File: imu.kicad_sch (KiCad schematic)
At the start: 6 parts, among them U6 LSM9DS1

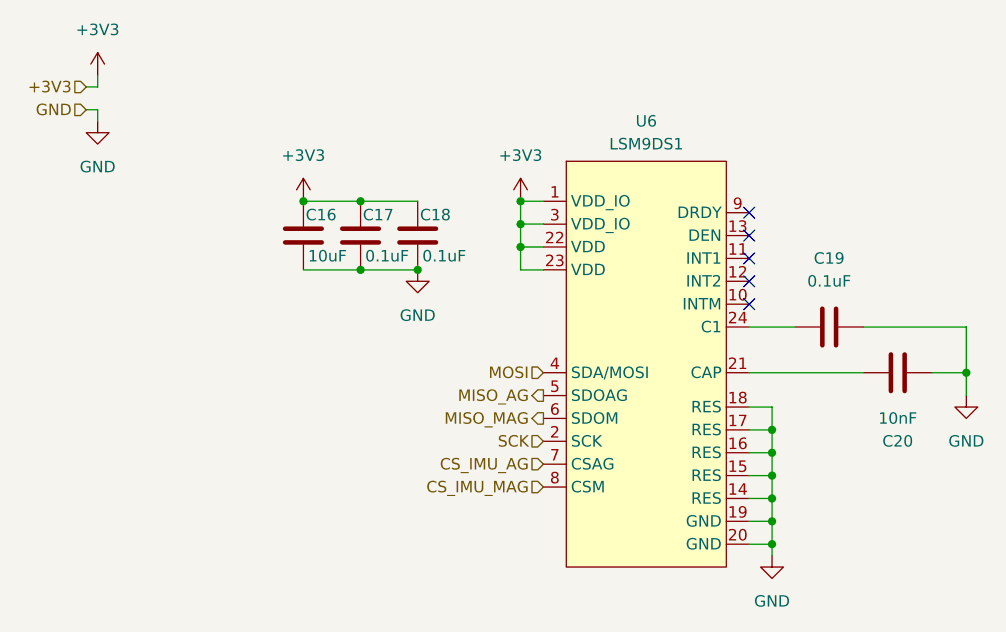
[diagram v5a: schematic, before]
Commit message: Radio footprint selection
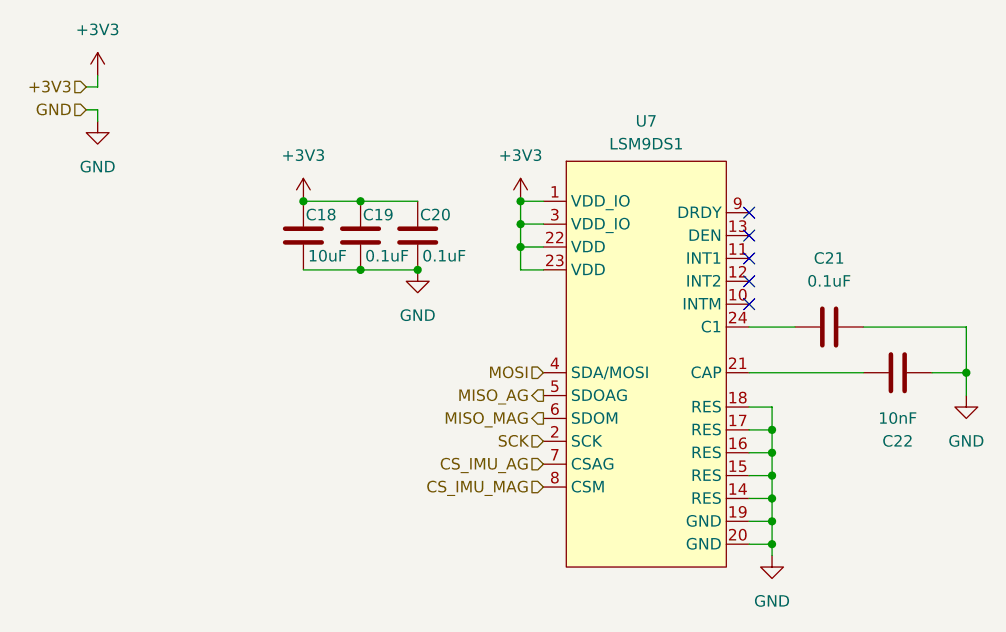
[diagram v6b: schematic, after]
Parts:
- renumbered C16 to C18, C17 to C19, C18 to C20, C19 to C21, C20 to C22, U6 to U7
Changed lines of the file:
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@@
 		(on_board yes)
 		(dnp no)
-		(property "Reference" "C16"
+		(property "Reference" "C18"
 			(at 76.454 49.784 0)
 			(effects
@@
 			(project ""
 				(path "/2c2eadf0-5503-4531-8753-1a232087fe8c/b9b0c40a-7771-4bc1-adbf-abe0201c34d0/6214bd7c-f0f2-4cad-9d95-7bb7bb29e083"
-					(reference "C16")
+					(reference "C18")
 					(unit 1)
 				)
@@
 		(dnp no)
 		(fields_autoplaced yes)
-		(property "Reference" "U6"
+		(property "Reference" "U7"
 			(at 114.3 39.37 0)
 			(effects
@@
 			(project ""
 				(path "/2c2eadf0-5503-4531-8753-1a232087fe8c/b9b0c40a-7771-4bc1-adbf-abe0201c34d0/6214bd7c-f0f2-4cad-9d95-7bb7bb29e083"
-					(reference "U6")
+					(reference "U7")
 					(unit 1)
 				)
@@
 		(dnp no)
 		(fields_autoplaced yes)
-		(property "Reference" "#PWR070"
+		(property "Reference" "#PWR076"
 			(at 76.2 52.07 0)
 			(effects
@@
 			(project ""
 				(path "/2c2eadf0-5503-4531-8753-1a232087fe8c/b9b0c40a-7771-4bc1-adbf-abe0201c34d0/6214bd7c-f0f2-4cad-9d95-7bb7bb29e083"
-					(reference "#PWR070")
+					(reference "#PWR076")
 					(unit 1)
 				)
@@
 		(dnp no)
 		(fields_autoplaced yes)
-		(property "Reference" "#PWR071"
+		(property "Reference" "#PWR077"
 			(at 100.33 52.07 0)
 			(effects
@@
 			(project ""
 				(path "/2c2eadf0-5503-4531-8753-1a232087fe8c/b9b0c40a-7771-4bc1-adbf-abe0201c34d0/6214bd7c-f0f2-4cad-9d95-7bb7bb29e083"
-					(reference "#PWR071")
+					(reference "#PWR077")
 					(unit 1)
 				)
@@
 		(dnp no)
 		(fields_autoplaced yes)
-		(property "Reference" "#PWR069"
+		(property "Reference" "#PWR075"
 			(at 53.34 45.72 0)
 			(effects
@@
 			(project ""
 				(path "/2c2eadf0-5503-4531-8753-1a232087fe8c/b9b0c40a-7771-4bc1-adbf-abe0201c34d0/6214bd7c-f0f2-4cad-9d95-7bb7bb29e083"
-					(reference "#PWR069")
+					(reference "#PWR075")
 					(unit 1)
 				)
@@
 		(dnp no)
 		(fields_autoplaced yes)
-		(property "Reference" "#PWR074"
+		(property "Reference" "#PWR080"
 			(at 128.27 93.98 0)
 			(effects
@@
 			(project ""
 				(path "/2c2eadf0-5503-4531-8753-1a232087fe8c/b9b0c40a-7771-4bc1-adbf-abe0201c34d0/6214bd7c-f0f2-4cad-9d95-7bb7bb29e083"
-					(reference "#PWR074")
+					(reference "#PWR080")
 					(unit 1)
 				)
@@
 		(dnp no)
 		(fields_autoplaced yes)
-		(property "Reference" "#PWR073"
+		(property "Reference" "#PWR079"
 			(at 149.86 76.2 0)
 			(effects
@@
 			(project ""
 				(path "/2c2eadf0-5503-4531-8753-1a232087fe8c/b9b0c40a-7771-4bc1-adbf-abe0201c34d0/6214bd7c-f0f2-4cad-9d95-7bb7bb29e083"
-					(reference "#PWR073")
+					(reference "#PWR079")
 					(unit 1)
 				)
@@
 		(on_board yes)
 		(dnp no)
-		(property "Reference" "C18"
+		(property "Reference" "C20"
 			(at 89.154 49.784 0)
 			(effects
@@
 			(project ""
 				(path "/2c2eadf0-5503-4531-8753-1a232087fe8c/b9b0c40a-7771-4bc1-adbf-abe0201c34d0/6214bd7c-f0f2-4cad-9d95-7bb7bb29e083"
-					(reference "C18")
+					(reference "C20")
 					(unit 1)
 				)
@@
 		(on_board yes)
 		(dnp no)
-		(property "Reference" "C17"
+		(property "Reference" "C19"
 			(at 82.804 49.784 0)
 			(effects
@@
 			(project ""
 				(path "/2c2eadf0-5503-4531-8753-1a232087fe8c/b9b0c40a-7771-4bc1-adbf-abe0201c34d0/6214bd7c-f0f2-4cad-9d95-7bb7bb29e083"
-					(reference "C17")
+					(reference "C19")
 					(unit 1)
 				)
@@
 		(dnp no)
 		(fields_autoplaced yes)
-		(property "Reference" "C19"
+		(property "Reference" "C21"
 			(at 134.62 54.61 90)
 			(effects
@@
 			(project ""
 				(path "/2c2eadf0-5503-4531-8753-1a232087fe8c/b9b0c40a-7771-4bc1-adbf-abe0201c34d0/6214bd7c-f0f2-4cad-9d95-7bb7bb29e083"
-					(reference "C19")
+					(reference "C21")
 					(unit 1)
 				)
@@
 		(on_board yes)
 		(dnp no)
-		(property "Reference" "C20"
+		(property "Reference" "C22"
 			(at 142.24 74.93 90)
 			(effects
@@
 			(project ""
 				(path "/2c2eadf0-5503-4531-8753-1a232087fe8c/b9b0c40a-7771-4bc1-adbf-abe0201c34d0/6214bd7c-f0f2-4cad-9d95-7bb7bb29e083"
-					(reference "C20")
+					(reference "C22")
 					(unit 1)
 				)
@@
 		(dnp no)
 		(fields_autoplaced yes)
-		(property "Reference" "#PWR072"
+		(property "Reference" "#PWR078"
 			(at 88.9 62.23 0)
 			(effects
@@
 			(project ""
 				(path "/2c2eadf0-5503-4531-8753-1a232087fe8c/b9b0c40a-7771-4bc1-adbf-abe0201c34d0/6214bd7c-f0f2-4cad-9d95-7bb7bb29e083"
-					(reference "#PWR072")
+					(reference "#PWR078")
 					(unit 1)
 				)
@@
 		(dnp no)
 		(fields_autoplaced yes)
-		(property "Reference" "#PWR068"
+		(property "Reference" "#PWR074"
 			(at 53.34 38.1 0)
 			(effects
@@
 			(project ""
 				(path "/2c2eadf0-5503-4531-8753-1a232087fe8c/b9b0c40a-7771-4bc1-adbf-abe0201c34d0/6214bd7c-f0f2-4cad-9d95-7bb7bb29e083"
-					(reference "#PWR068")
-					(unit 1)
-				)
+					(reference "#PWR074")
+					(unit 1)
+				)

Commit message: Addeed part numbers
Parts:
- C18: LCSC (none) -> C96446
- C19, C20, C21: LCSC (none) -> C14663
- C22: LCSC (none) -> C1589
- U7: LCSC (none) -> C2655096
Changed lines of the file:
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@@
+			)
+		)
+		(property "LCSC" "C96446"
+			(at 76.2 52.07 0)
+			(effects
+				(font
+					(size 1.27 1.27)
+				)
+				(hide yes)
 			)
 		)
@@
 			)
 		)
+		(property "LCSC" "C2655096"
+			(at 101.6 40.64 0)
+			(effects
+				(font
+					(size 1.27 1.27)
+				)
+				(hide yes)
+			)
+		)
 		(pin "3"
 		)
@@
 			)
 		)
+		(property "LCSC" "C14663"
+			(at 88.9 52.07 0)
+			(effects
+				(font
+					(size 1.27 1.27)
+				)
+				(hide yes)
+			)
+		)
 		(pin "1"
 		)
@@
 		)
 		(property "Description" "Unpolarized capacitor"
+			(at 82.55 52.07 0)
+			(effects
+				(font
+					(size 1.27 1.27)
+				)
+				(hide yes)
+			)
+		)
+		(property "LCSC" "C14663"
 			(at 82.55 52.07 0)
 			(effects
@@
 			)
 		)
+		(property "LCSC" "C14663"
+			(at 134.62 62.23 90)
+			(effects
+				(font
+					(size 1.27 1.27)
+				)
+				(hide yes)
+			)
+		)
 		(pin "1"
 		)
@@
 			(effects
 				(font
+					(size 1.27 1.27)
+				)
+				(hide yes)
+			)
+		)
+		(property "LCSC" "C1589"
+			(at 142.24 67.31 90)
+			(effects
+				(font
